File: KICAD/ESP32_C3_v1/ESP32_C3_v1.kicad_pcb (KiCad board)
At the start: 2 copper layers, 90 x 70 mm, 34 parts, among them J1 USB Serial/JTAG, J10 Peer_UART, J2 Port_Header, J3 Grove I2C, J4 ADC_Header, J5 (T2) Screw_Terminal_01x03, J6 (T1) Screw_Terminal_01x03, J7 J_AUTO (Reset Automation), J8 External 5V Power, J9 SPI (Optional Module Flash)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

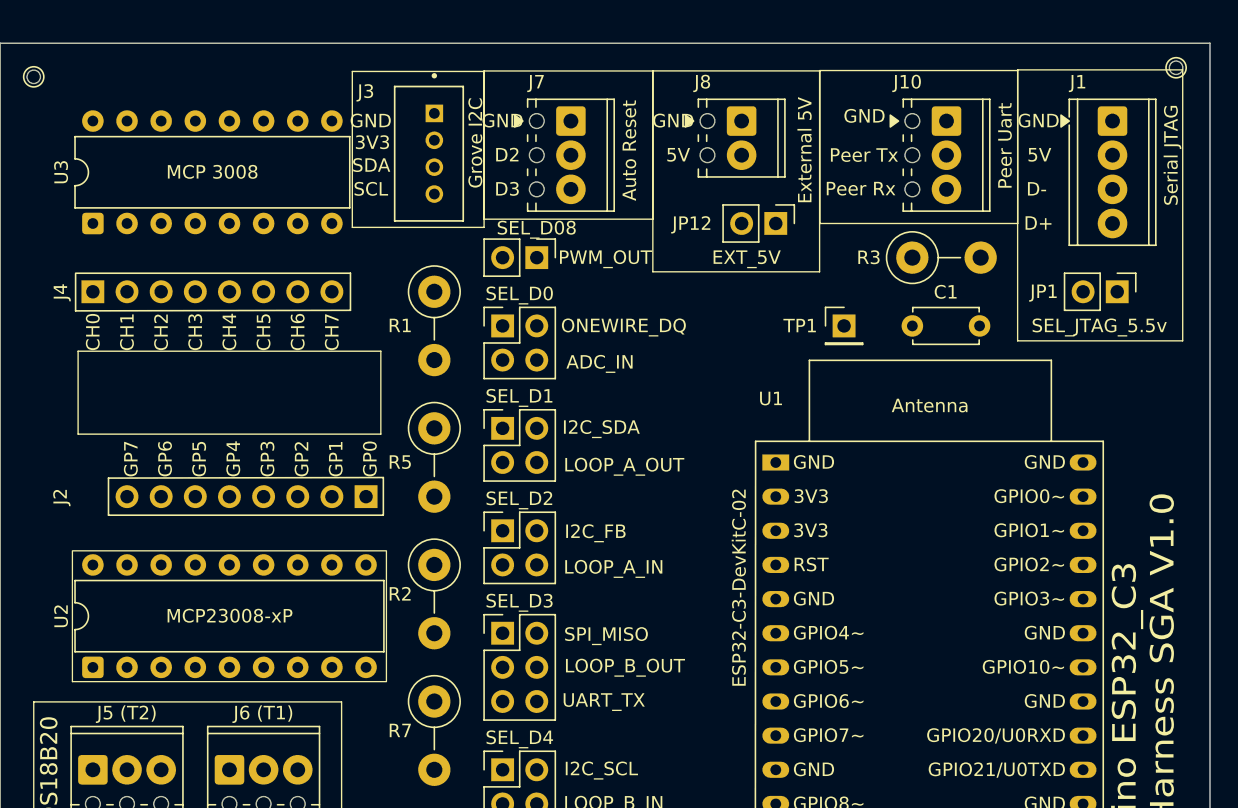
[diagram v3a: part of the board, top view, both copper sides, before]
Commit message: Refine ESP32-C3 v1.1 PCB layout
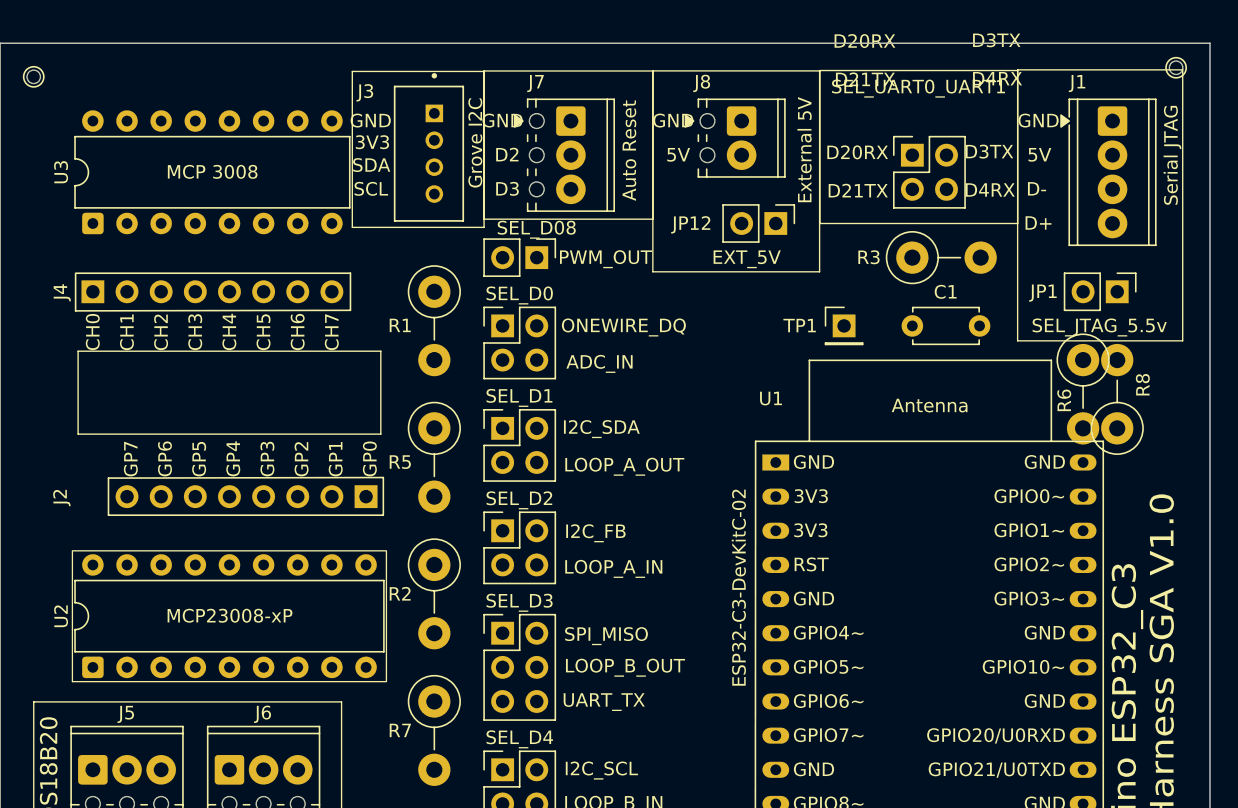
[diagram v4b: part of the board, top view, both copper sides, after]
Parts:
- removed J10: Peer_UART, ESP32_C3_Harness:TerminalBlock_Phoenix_MPT-0,5-3-2.54_1x03_P2.54mm_Horizontal
- added R6: 470R, ESP32_C3_Harness:R_Axial_DIN0411_L9.9mm_D3.6mm_P5.08mm_Vertical, F.Cu at (150.6, 68.6)
- added R8: 470R, ESP32_C3_Harness:R_Axial_DIN0411_L9.9mm_D3.6mm_P5.08mm_Vertical, F.Cu at (153.1, 73.7)
- added SEL_UART0_UART1: D3TX-D20RX | D21TX-D4RX, ESP32_C3_Harness:PinHeader_2x02_RowLetter_P2.54mm_Vertical, F.Cu at (137.9, 53.3)
- J5: renamed from J5 (T2)
- J6: renamed from J6 (T1)
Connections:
- SEL_D3 pad b3: /PEER_RX_FROM_D3_UART_TX -> /D3_UART1_TX
- SEL_D4 pad b3: /PEER_TX_TO_D4_UART_RX -> /D4_UART1_RX
- U1 pad 21: unconnected-(U1-GPIO21/U0TXD-Pad21) -> Net-(U1-GPIO21/U0TXD)
- U1 pad 22: unconnected-(U1-GPIO20/U0RXD-Pad22) -> Net-(U1-GPIO20/U0RXD)
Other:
- board text added: "D20RX"
- board text added: "D21TX"
- board text added: "D3TX"
- board text added: "D4RX"
- board text added: "R6"
- board text added: "R8"
- board text added: "SEL_UART0_UART1"
- board text removed: "Peer Rx"
- board text removed: "Peer Tx"
- board text removed: "Peer Uart"

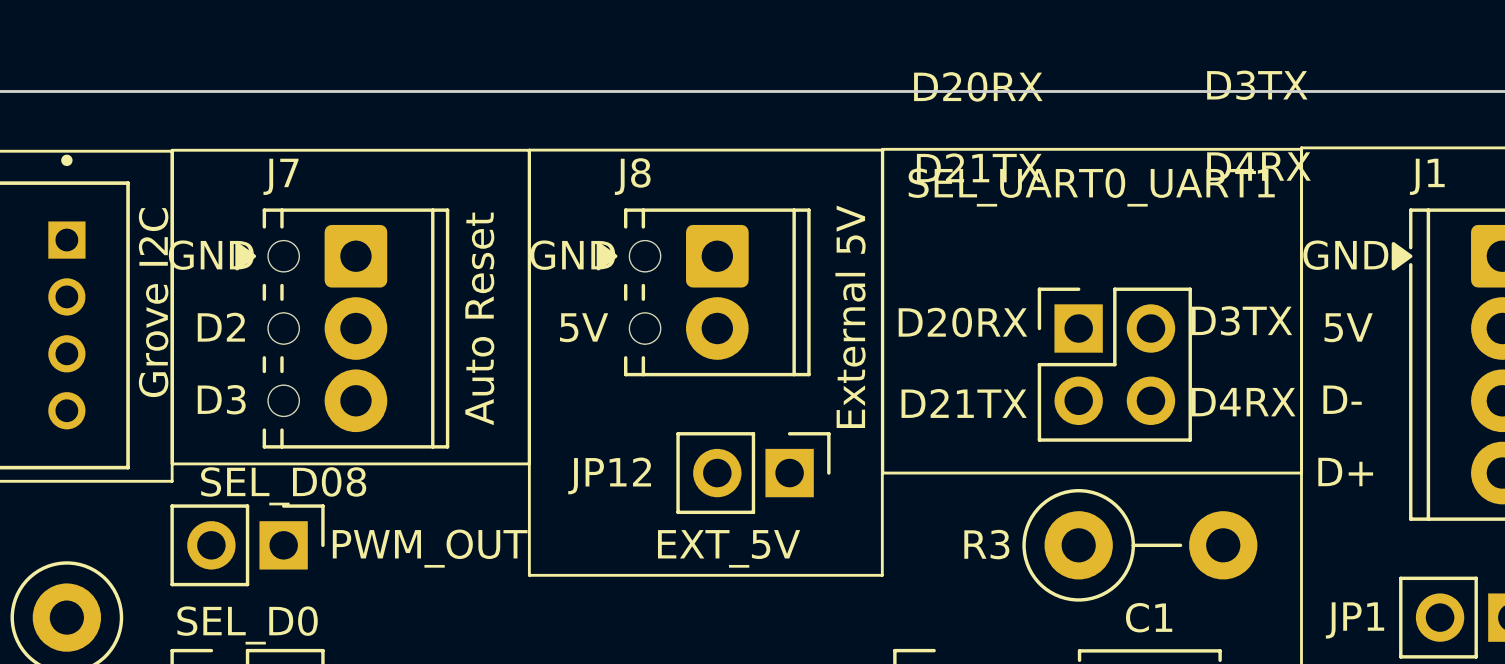
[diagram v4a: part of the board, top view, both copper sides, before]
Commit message: Refine ESP32-C3 v1.1 J10 UART schematic and PCB
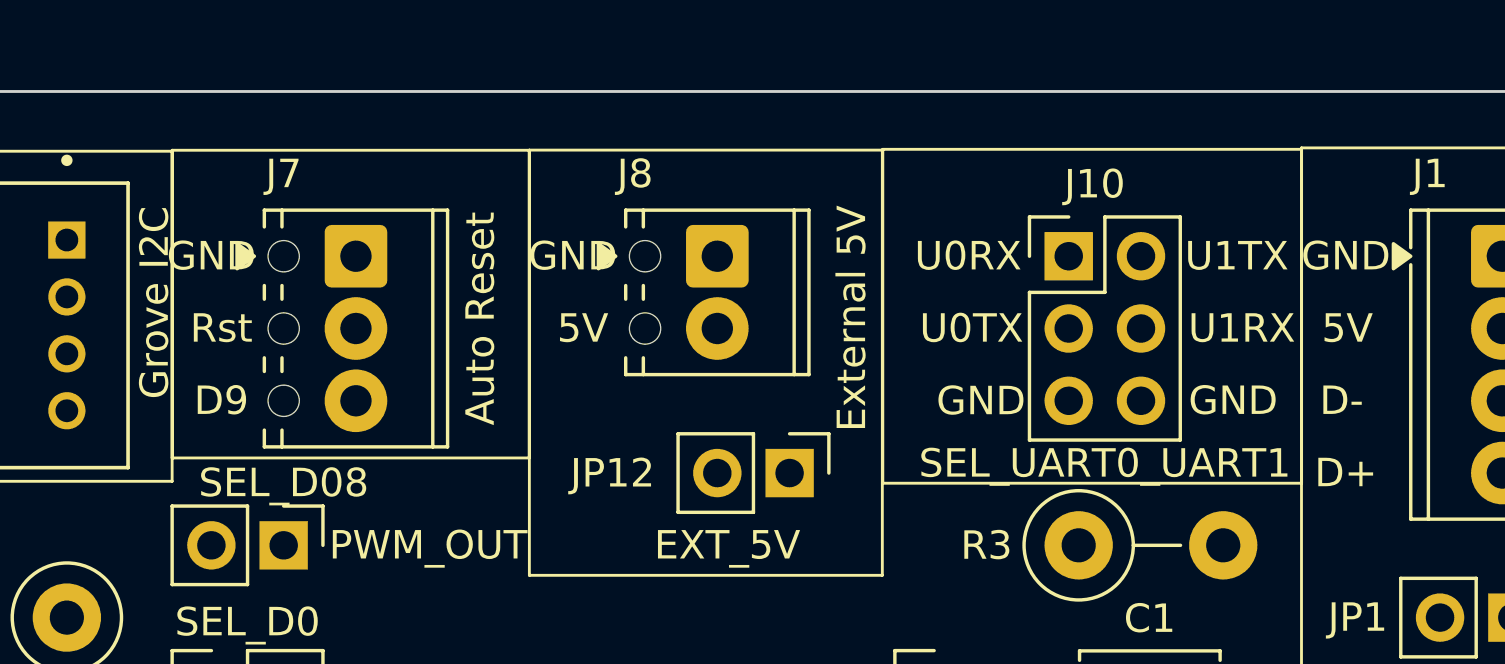
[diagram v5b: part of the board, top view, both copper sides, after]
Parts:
- removed SEL_UART0_UART1: D3TX-D20RX | D21TX-D4RX, ESP32_C3_Harness:PinHeader_2x02_RowLetter_P2.54mm_Vertical
- added J10: SEL_UART0_UART1, ESP32_C3_Harness:PinHeader_2x03_RowLetter_P2.54mm_Vertical, F.Cu at (137.5, 50.8)
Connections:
- net Net-(J7-Pin_2) renamed /Reset
- net Net-(J7-Pin_3) renamed /GPIO09
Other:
- board text added: "D20U0RX"
- board text added: "D21U0TX"
- board text added: "D3U1TX"
- board text added: "D4U1RX"
- board text added: "D9"
- board text added: "Rst"
- board text added: "U0RX"
- board text added: "U0TX"
- board text added: "U1RX"
- board text added: "U1TX"
- board text removed: "D20RX"
- board text removed: "D21TX"
- board text removed: "D3TX"
- board text removed: "D4RX"
